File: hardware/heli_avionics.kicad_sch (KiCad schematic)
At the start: 19 parts, among them J1 Pin_Header_2x3, J7 JST_ZH_01x02, SW1 Reset, U1 ATmega4808-A

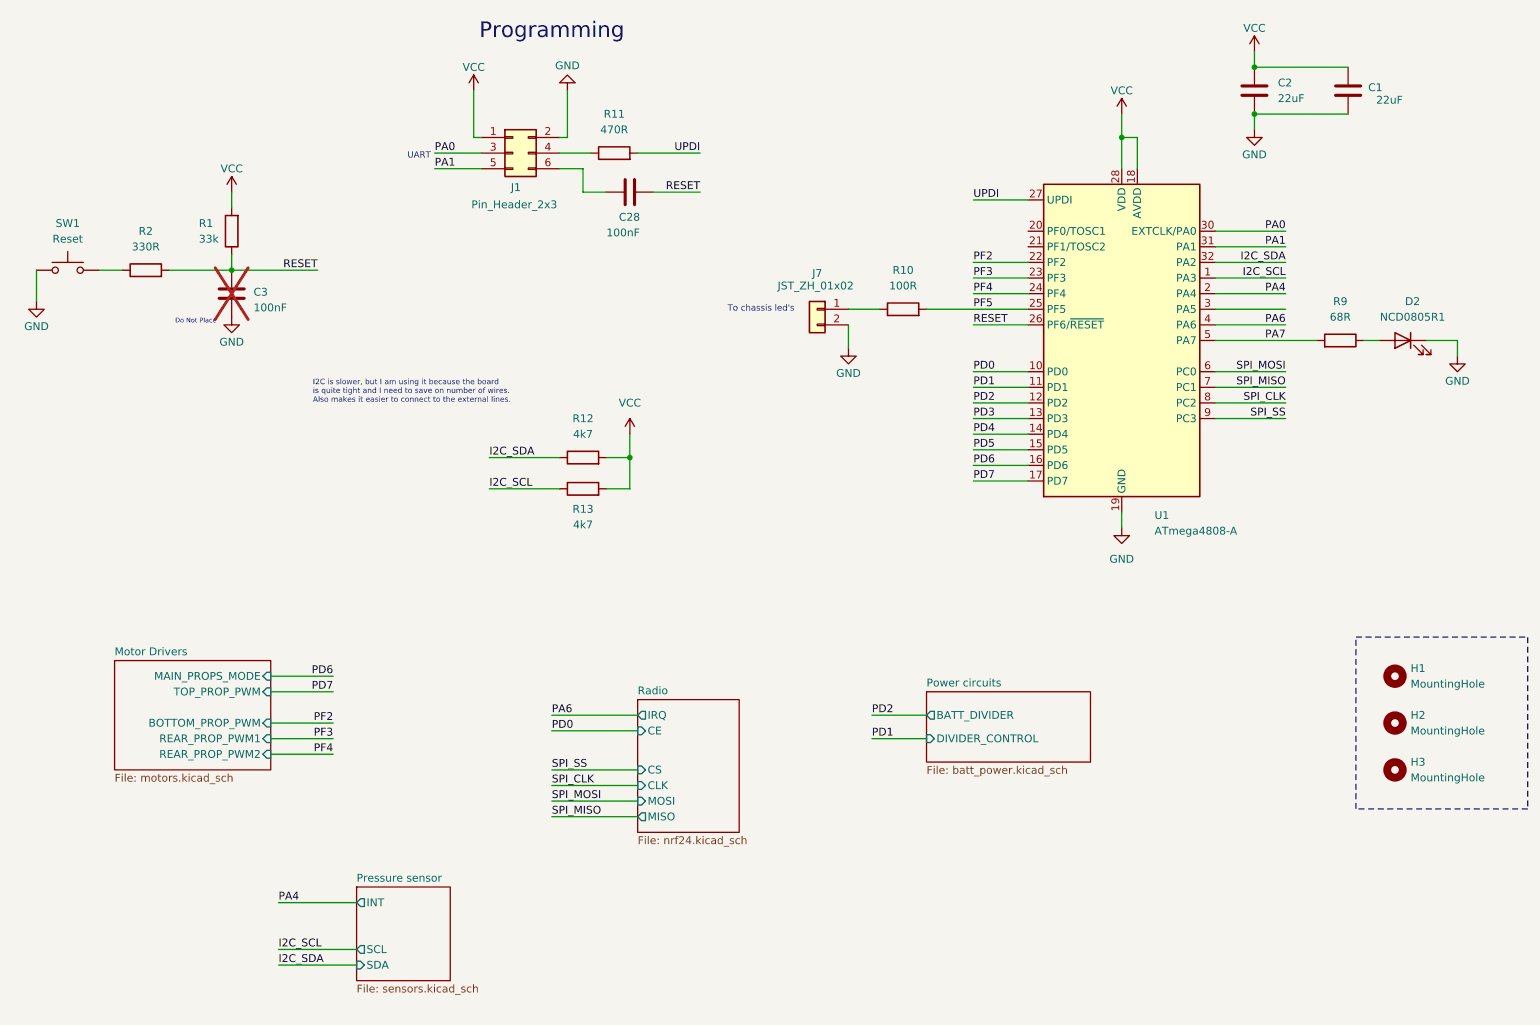
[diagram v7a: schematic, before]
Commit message: Added pin headers for external connections (PA6 and I2C)
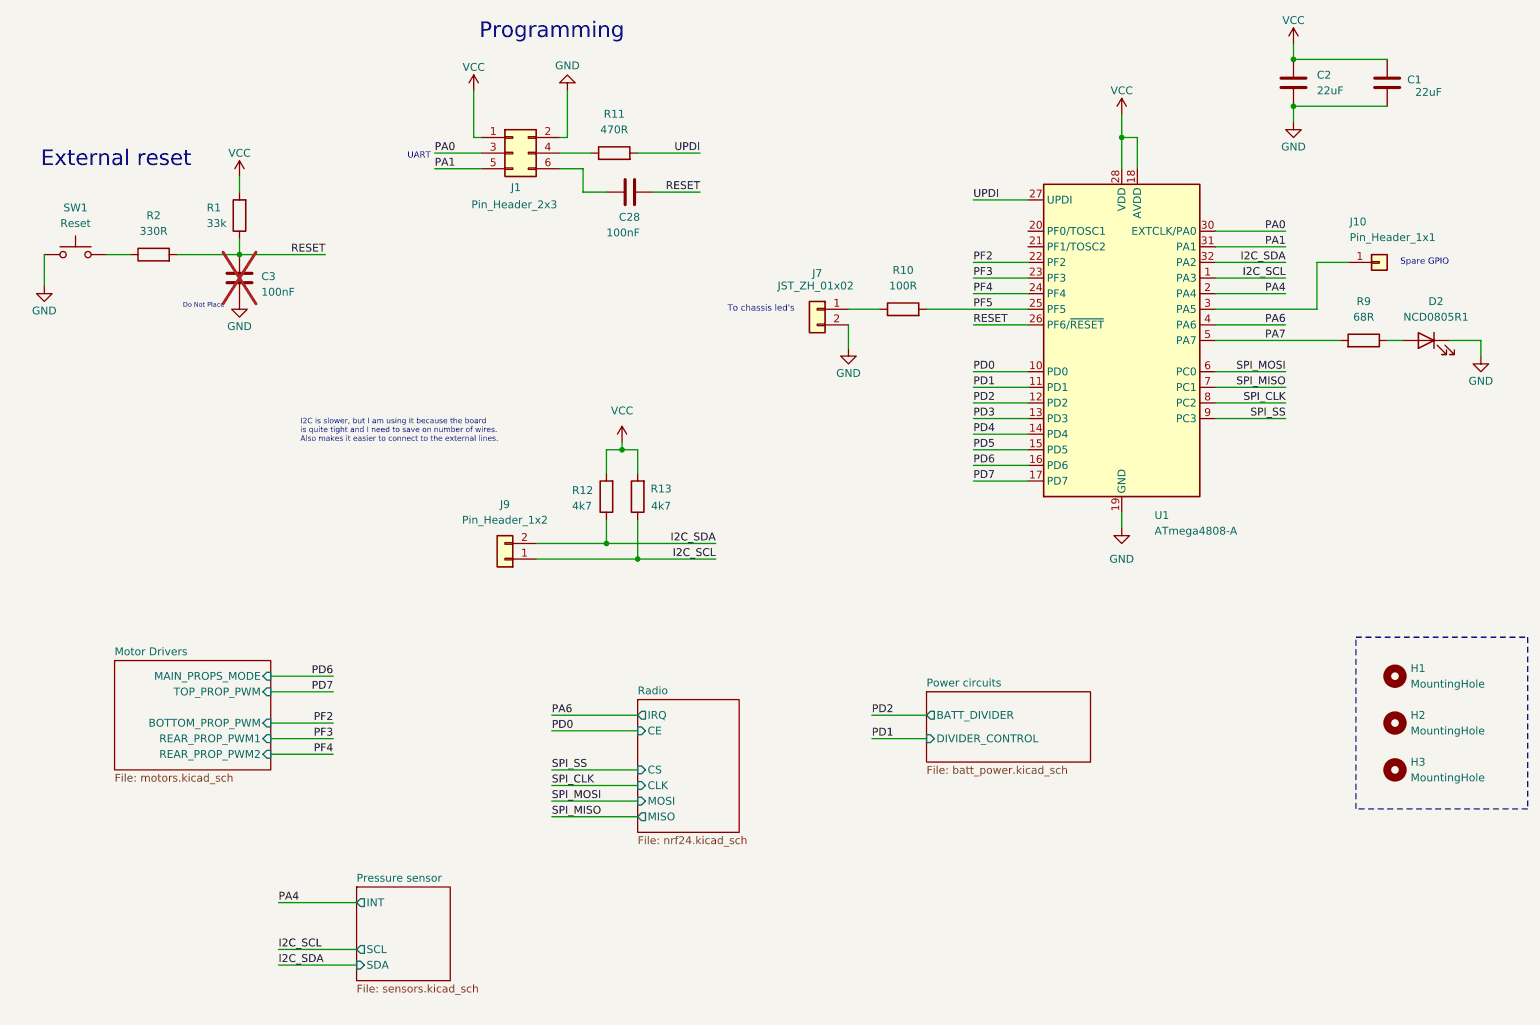
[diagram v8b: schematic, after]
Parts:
- added J10: Pin_Header_1x1, Connector_PinHeader_2.54mm:PinHeader_1x01_P2.54mm_Vertical, symbol Connector_Generic:Conn_01x01
- added J9: Pin_Header_1x2, Connector_PinHeader_2.54mm:PinHeader_1x02_P2.54mm_Vertical, symbol Connector_Generic:Conn_01x02
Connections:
- net I2C_SCL: now also J9.1 (Pin_1)
- net I2C_SDA: now also J9.2 (Pin_2)
- net at U1.3 (PA5): now also J10.1 (Pin_1)
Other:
- note added: "External reset"
- note added: "Spare GPIO"
- moved on the sheet: C1, C2, C3, D2, R1, R12, R13, R2, R9, SW1
